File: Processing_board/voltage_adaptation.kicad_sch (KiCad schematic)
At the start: 20 parts, among them J8 Conn_01x03_Pin, J9 Conn_01x03_Pin, Q1 DMP3056LSS-13, U5 LD1117S50TR_SOT223, U6 LD1117S33TR_SOT223, U7 LD1117DT18TR

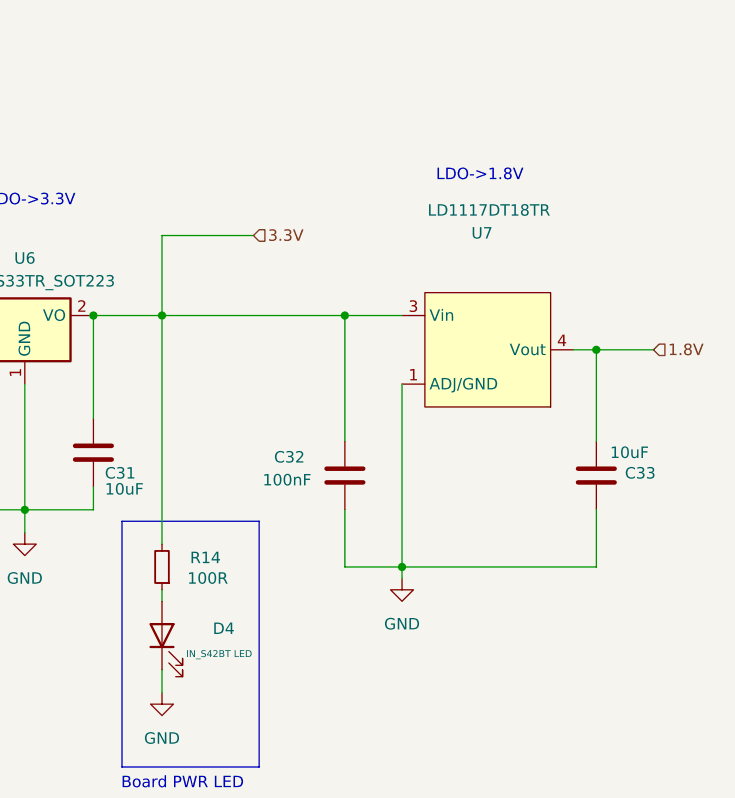
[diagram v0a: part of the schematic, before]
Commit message: feat: implemented voltage adaptation circuit
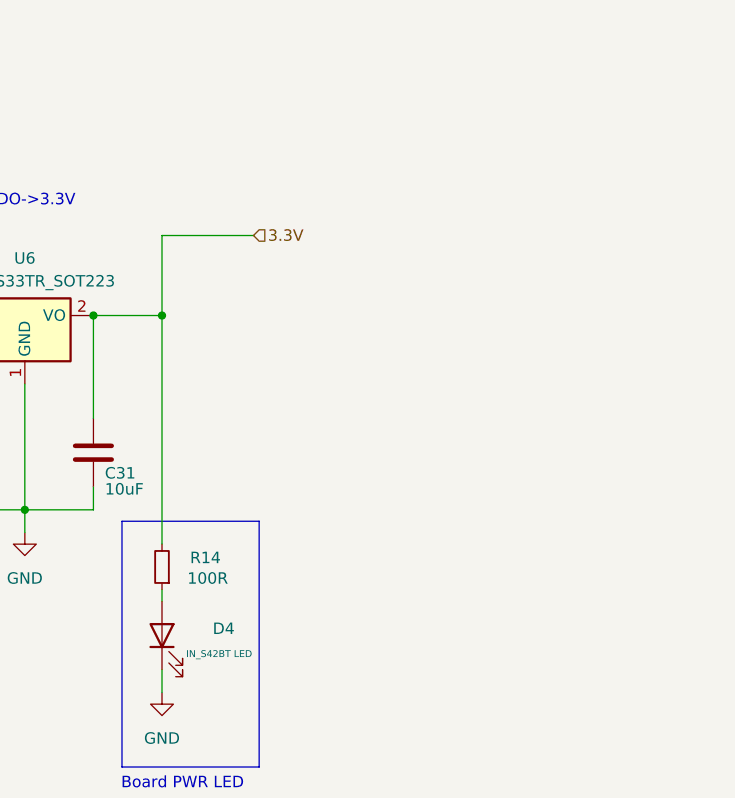
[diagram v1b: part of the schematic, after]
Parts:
- removed C32: 100nF, Capacitor_SMD:C_0402_1005Metric, symbol Device:C
- removed C33: 10uF, Capacitor_SMD:C_0402_1005Metric, symbol Device:C
- removed U7: LD1117DT18TR, LD1117DT18TR:TO228P972X240-3N, symbol Custom_Symbol_Library_Npulse:LD1117DT18TR
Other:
- note removed: "LDO->1.8V"

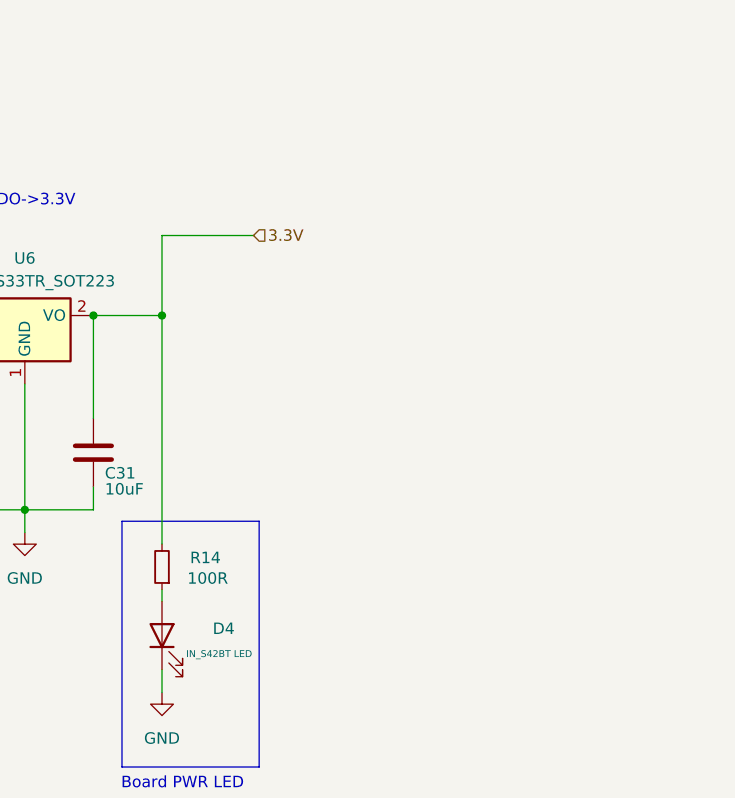
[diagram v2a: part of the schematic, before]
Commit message: fix: changed low-pass filter
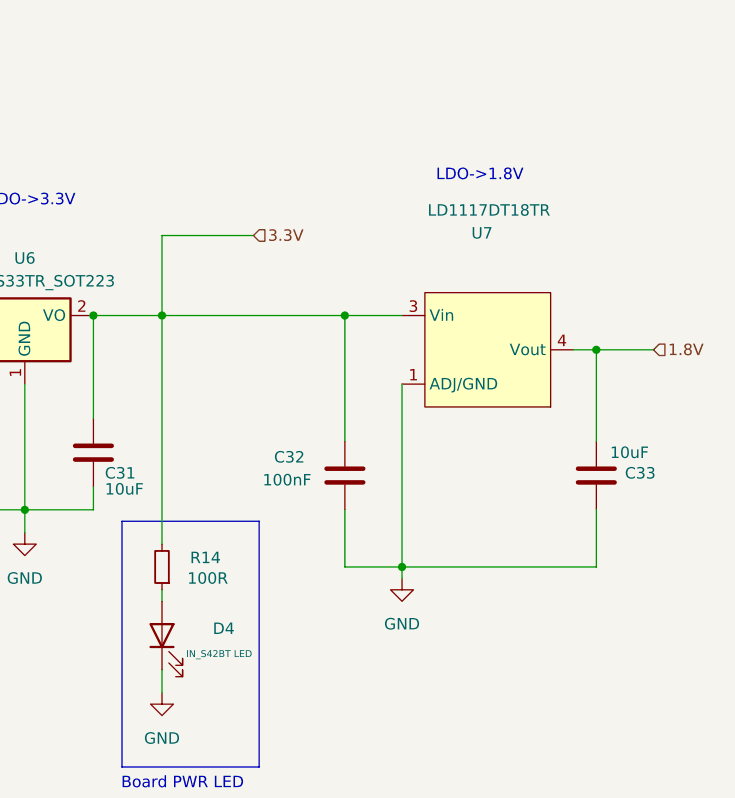
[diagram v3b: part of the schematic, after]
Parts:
- added C32: 100nF, Capacitor_SMD:C_0402_1005Metric, symbol Device:C
- added C33: 10uF, Capacitor_SMD:C_0402_1005Metric, symbol Device:C
- added U7: LD1117DT18TR, LD1117DT18TR:TO228P972X240-3N, symbol Custom_Symbol_Library_Npulse:LD1117DT18TR
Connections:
- net 3.3V: now also C32.1, U7.3 (Vin)
- net GND: now also C32.2, C33.1, U7.1 (ADJ/GND)
- new net 1.8V: C33.2, U7.4 (Vout)
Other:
- note added: "LDO->1.8V"
